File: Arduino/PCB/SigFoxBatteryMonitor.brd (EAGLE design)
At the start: 100 x 100 mm, 55 parts, among them IC1 BD6211F, IC2 BD6211F, IC3 7805TV, Q1 MOSFET-NCHANNELFDS6630A, Q2 MOSFET-NCHANNELFDS6630A, Q3 MOSFET-NCHANNELFDS6630A, U1 INA219AIDCNRSOIC, X2 PN87520-S

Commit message: Version 1.0 PCB.
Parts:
- added D3, D4: MBRA140, SparkFun-DiscreteSemi:SMA-DIODE
- added JP12, JP13, JP14: (no value), SparkFun-Connectors:1X02
- added JP15, JP16, JP17, JP18, JP19, JP20, JP21, JP22, JP23, JP25, JP26, JP27, JP28, JP29, JP30, JP31: (no value), SparkFun-Connectors:1X05_NO_SILK
- added JP32, JP33: (no value), SparkFun-Connectors:1X05
- added R10, R9: 100k, SparkFun-Resistors:0805
- added R11, R12, R13, R14, R15, R16: (no value), SparkFun-Resistors:0805
- added TP4: 5v, testpad:TP15R
- C9: value 1.0uF -> 0.1uF
- JP7: device SparkFun-Connectors:MOLEX-1X3 -> SparkFun-Connectors:MOLEX-1X4
- JP8: device SparkFun-Connectors:MOLEX-1X3 -> SparkFun-Connectors:1X01
- Q1, Q2, Q3: value MOSFET-NCHANNELFDS6630A -> IRF7413Z
- R1: value (none) -> 1k5
- R3, R5, R7: value (none) -> 10R
- R4, R6, R8: value (none) -> 10k
- U2: value (none) -> 1117st33
- moved JP8 68.7 mm to (15.6, 93.2), turned to 180 degrees
- moved TP1 17.1 mm to (1.91, 15.9)
- moved FRAME1 8.47 mm to (19.7, -15.9)
- moved C8 7.01 mm to (74.3, 14.6)
- moved R4 6.98 mm to (78.7, 51.1), turned to 0 degrees
- moved C7 6.70 mm to (58.1, 8.26), turned to 180 degrees
- moved R6 6.67 mm to (79.1, 62.2), turned to 180 degrees
- moved R8 6.35 mm to (79.4, 73.0), turned to 0 degrees
- moved C10 4.58 mm to (68.6, 7.62), turned to 270 degrees
- moved JP10 4.45 mm to (16.5, 44.5)
- moved JP11 4.45 mm to (44.5, 77.5)
- moved U$3 4.45 mm to (17.8, 31.8)
- moved C9 4.02 mm to (65.4, 7.62)
- moved R1 4.02 mm to (13.3, 81.9)
- moved CHARGE 2.86 mm to (95.9, 27.5)
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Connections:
- new net A5: JP10.8, R13.2, R14.1, U$3.A5
- new net A6: JP10.7, R15.2, R16.1, U$3.A6
- new net N$14: D3.C, JP12.2
- new net N$16: JP8.1, R9.2
- new net N$18: D2.A, JP14.1
- new net N$19: C3.1, C4.1, D4.A, TP4.TP, U2.2, U2.4
- net +3V3: now also D4.C, JP12.1; no longer C3.1, C4.1, JP7.3, JP8.3, U2.2, U2.4
- net 5V: now also JP13.2, JP7.4
- net ANALOG_0: now also R10.2, R9.1
- net ANALOG_5: now also R13.1; no longer JP10.8, U$3.A5
- net ANALOG_6: now also JP7.3, R15.1; no longer JP10.7, JP8.2, U$3.A6
- net ARDUINO_5V: now also JP13.1
- net GND: now also JP33.1, JP33.2, JP33.3, JP33.4, JP33.5, R10.1, R14.2, R16.2; no longer JP8.1
- net SCL: now also R12.1
- net SDA: now also R11.1
- net VCC: now also D3.A, JP32.1, JP32.2, JP32.3, JP32.4, JP32.5, R11.2, R12.2
- net V_BATT: now also JP14.2; no longer D2.A
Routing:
- net VCC: track 104.2 -> 150.8 mm
- net V_BATT: track 150.2 -> 106.4 mm, vias 1 -> 0
- net ANALOG_6: track 47.1 -> 4.81 mm
- net A5: track 0.00 -> 35.4 mm
- net A6: track 0.00 -> 34.8 mm
- net 5V: track 125.4 -> 159.8 mm, vias 0 -> 2
- net ANALOG_5: track 36.6 -> 4.81 mm
- net N$18: track 0.00 -> 31.6 mm
- net N$19: track 0.00 -> 30.9 mm
- net +3V3: track 212.8 -> 183.8 mm, vias 10 -> 6
- net ANALOG_0: track 3.81 -> 26.4 mm
- net N$14: track 0.00 -> 7.35 mm
- net ARDUINO_5V: track 3.81 -> 9.84 mm
- net N$7: track 23.2 -> 17.2 mm
- net ANALOG_1: track 24.8 -> 29.6 mm
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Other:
- outline, holes or cut-outs redrawn
- board text added: "5"
- board text added: "5V"
- board text added: "6"
- board text added: "A0"
- board text added: "A1"
- board text added: "A2"
- board text added: "A3"
- board text added: "A4"
- board text added: "A5"
- board text added: "A6"
- board text added: "AREF"
- board text added: "Batt Sense +ve"
- board text added: "Connect for Arduino 3v3 source."
- board text added: "Connect to power from Arudino USB"
- board text added: "Connect to power from Battery"
- board text added: "D0"
- board text added: "D1"
- board text added: "D6"
- board text added: "D7"
- board text added: "MISO"
- board text added: "MOSI"
- board text added: "RST"
- board text added: "RX"
- board text added: "SCK"
- board text added: "SCL"
- board text added: "SDA"
- board text added: "SigFix Remote System Monitor"
- board text added: "TX"
- board text added: "VIN"
- board text added: "~D2"
- board text added: "~D3"
- board text added: "~D4"
- board text added: "~D5"
- board text removed: "Analog 6"
- board text removed: "SigFix Battery Monitor"

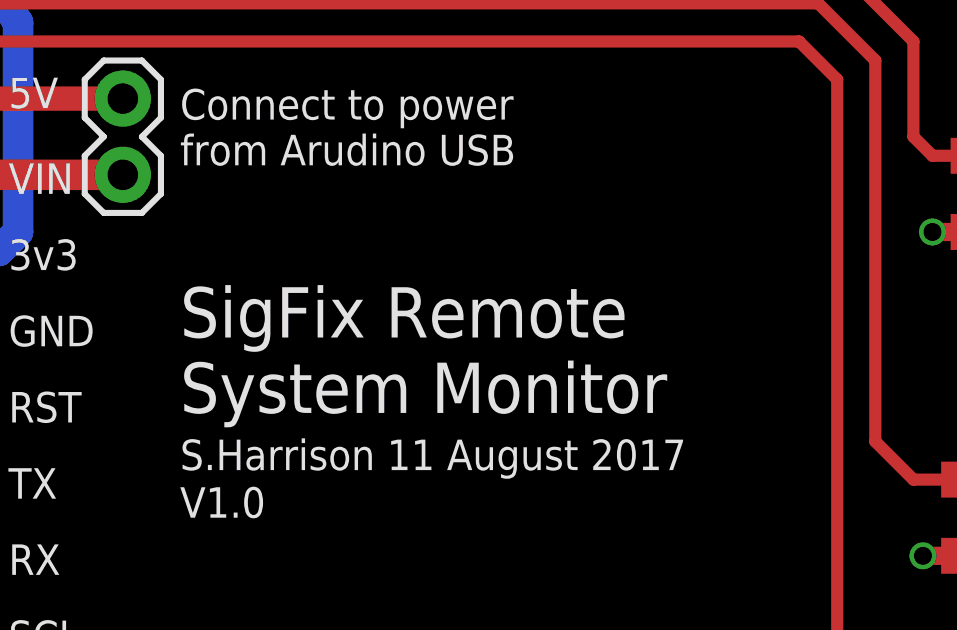
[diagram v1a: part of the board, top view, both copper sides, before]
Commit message: Fixed type on silkscreen and improved layout of schematic.
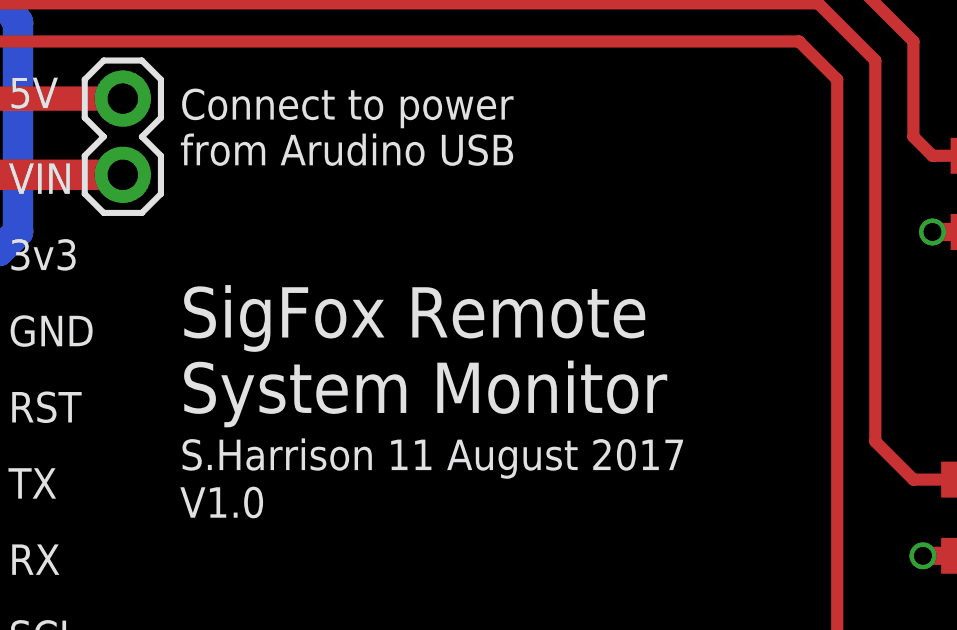
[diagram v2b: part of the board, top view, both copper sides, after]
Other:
- board text added: "SigFox Remote System Monitor"
- board text removed: "SigFix Remote System Monitor"
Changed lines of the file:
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@@
 <text x="99.06" y="74.295" size="1.016" layer="25" ratio="12" rot="R90">GND</text>
 <text x="52.3875" y="65.0875" size="1.016" layer="25" ratio="12">S.Harrison 11 August 2017</text>
-<text x="52.3875" y="66.9925" size="1.6764" layer="25" ratio="12">SigFix Remote
+<text x="52.3875" y="66.9925" size="1.6764" layer="25" ratio="12">SigFox Remote
 System Monitor</text>
 <text x="48.895" y="98.1075" size="1.016" layer="25" ratio="12">https://github.com/Tinamous/BatteryMonitor</text>
